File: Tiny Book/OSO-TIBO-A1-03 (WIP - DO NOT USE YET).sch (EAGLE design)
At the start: 103 parts, among them J2 10118193-0001LF, Q1 DMG341, Q2 IRLML0100, SW1 SPST_TACTILE_SWITCHRA-THRU, SW2 SPDT_SWITCH, U1 AP2112-3.3, U2 MCP73831T-2ACI/OT, U3 ATSAMD51G18A-MUT, U4 GD25Q16C (or GD25Q32C), U5 MAX4468EKAT, X1 JSTPH, X2 2x5 0.05" SWD

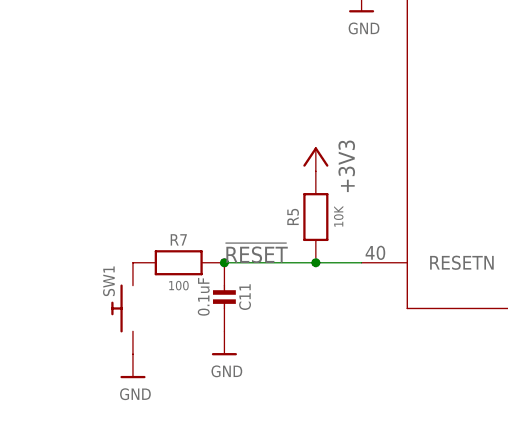
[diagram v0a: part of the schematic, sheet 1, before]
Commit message: surface mount reset button
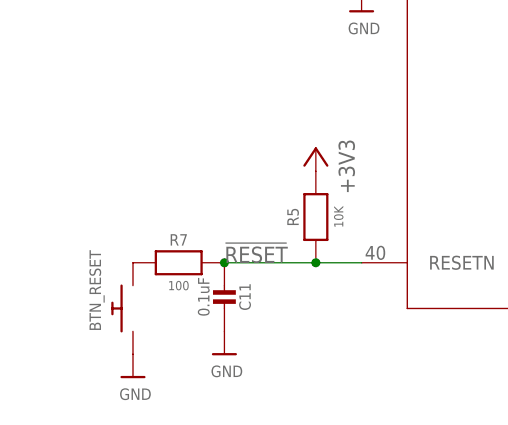
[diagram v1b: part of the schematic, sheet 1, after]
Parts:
- removed SW1: SPST_TACTILE_SWITCHRA-THRU, My Stuff:SPST_TACTILE_SWITCHRA-THRU
- added BTN_RESET: (no value), adafruit:SWITCH_PUSHBUTTONC&K_KSS
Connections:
- net GND: now also BTN_RESET.P$1; no longer SW1.P$1
- net N$1: now also BTN_RESET.P$2; no longer SW1.P$2
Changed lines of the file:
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@@
 <part name="SW2" library="My Stuff" deviceset="SPDT_SWITCH" device=""/>
 <part name="U$12" library="microbuilder" deviceset="GND" device=""/>
-<part name="SW1" library="My Stuff" deviceset="SPST_TACTILE_SWITCH" device="RA-THRU" value="SPST_TACTILE_SWITCHRA-THRU"/>
 <part name="+3V7" library="supply1" library_urn="urn:adsk.eagle:library:371" deviceset="+3V3" device=""/>
 <part name="+3V8" library="supply1" library_urn="urn:adsk.eagle:library:371" deviceset="+3V3" device=""/>
@@
 <part name="R5" library="microbuilder" deviceset="RESISTOR" device="0805_NOOUTLINE" value="10K"/>
 <part name="+3V6" library="supply1" library_urn="urn:adsk.eagle:library:371" deviceset="+3V3" device=""/>
+<part name="BTN_RESET" library="adafruit" deviceset="SWITCH_PUSHBUTTON" device="C&amp;K_KSS"/>
 </parts>
 <sheets>
@@
 <attribute name="VALUE" x="5.08" y="144.78" size="1.016" layer="96" font="vector" ratio="15" rot="R270" align="center"/>
 </instance>
-<instance part="SW1" gate="G$1" x="12.7" y="15.24" smashed="yes" rot="R90">
-<attribute name="NAME" x="10.668" y="16.51" size="1.27" layer="95" rot="R90"/>
-</instance>
 <instance part="U$24" gate="G$1" x="12.7" y="7.62" smashed="yes">
 <attribute name="VALUE" x="11.176" y="5.08" size="1.27" layer="96"/>
@@
 <instance part="+3V6" gate="G$1" x="33.02" y="33.02" smashed="yes" rot="MR0">
 <attribute name="VALUE" x="35.56" y="27.94" size="1.778" layer="96" rot="MR90"/>
+</instance>
+<instance part="BTN_RESET" gate="G$1" x="12.7" y="15.24" smashed="yes" rot="R90">
+<attribute name="NAME" x="9.144" y="12.7" size="1.27" layer="95" rot="R90"/>
+<attribute name="VALUE" x="14.986" y="12.7" size="1.27" layer="96" rot="R90"/>
 </instance>
 </instances>
@@
 <wire x1="238.76" y1="96.52" x2="243.84" y2="96.52" width="0.1524" layer="91"/>
 <junction x="243.84" y="96.52"/>
-</segment>
-<segment>
-<pinref part="U$24" gate="G$1" pin="GND"/>
-<pinref part="SW1" gate="G$1" pin="P$1"/>
 </segment>
 <segment>
@@
 <pinref part="U3" gate="A" pin="EPAD"/>
 <pinref part="U$3" gate="G$1" pin="GND"/>
+</segment>
+<segment>
+<pinref part="U$24" gate="G$1" pin="GND"/>
+<pinref part="BTN_RESET" gate="G$1" pin="P$1"/>
 </segment>
 </net>
@@
 </segment>
 </net>
-<net name="N$1" class="0">
-<segment>
-<pinref part="SW1" gate="G$1" pin="P$2"/>
-<pinref part="R7" gate="G$1" pin="1"/>
-</segment>
-</net>
 <net name="N$9" class="0">
 <segment>
@@
 </segment>
 </net>
+<net name="N$1" class="0">
+<segment>
+<pinref part="R7" gate="G$1" pin="1"/>
+<pinref part="BTN_RESET" gate="G$1" pin="P$2"/>
+</segment>
+</net>

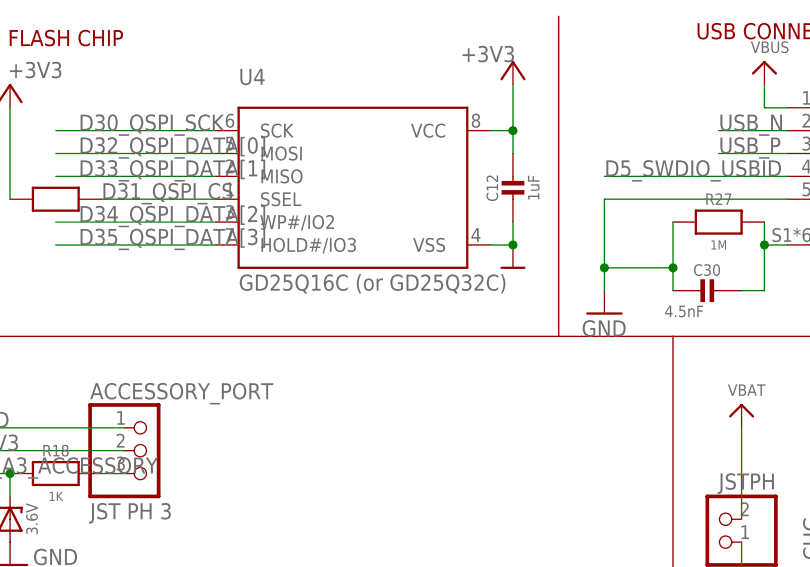
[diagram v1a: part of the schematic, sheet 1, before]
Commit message: use 4MB flash so babel can live there
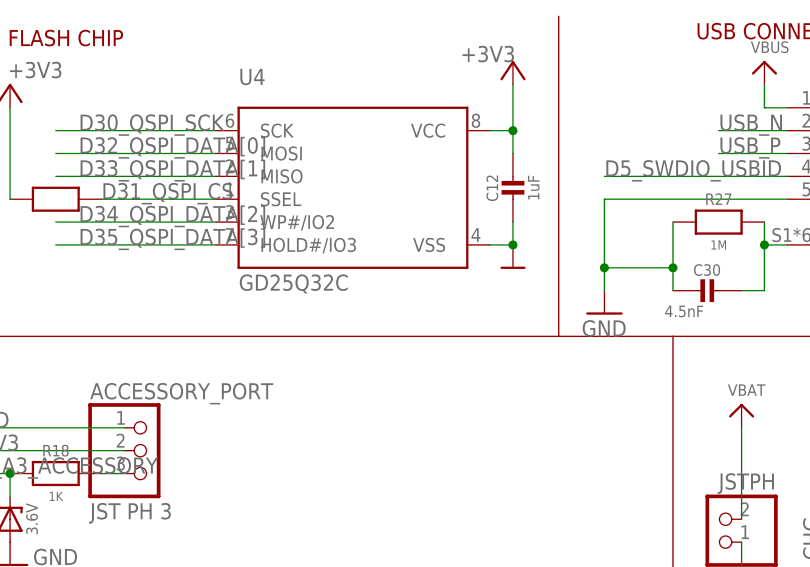
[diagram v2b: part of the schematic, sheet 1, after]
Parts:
- U4: value GD25Q16C (or GD25Q32C) -> GD25Q32C
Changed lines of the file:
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@@
 <part name="FID2" library="microbuilder" deviceset="FIDUCIAL" device="_1MM"/>
 <part name="U$24" library="microbuilder" deviceset="GND" device=""/>
-<part name="U4" library="Adafruit Feather M0 Express" deviceset="MICROBUILDER_SPIFLASH_SOIC8" device="" value="GD25Q16C (or GD25Q32C)"/>
+<part name="U4" library="Adafruit Feather M0 Express" deviceset="MICROBUILDER_SPIFLASH_SOIC8" device="" value="GD25Q32C"/>
 <part name="+3V15" library="supply1" library_urn="urn:adsk.eagle:library:371" deviceset="+3V3" device=""/>
 <part name="+3V16" library="supply1" library_urn="urn:adsk.eagle:library:371" deviceset="+3V3" device=""/>

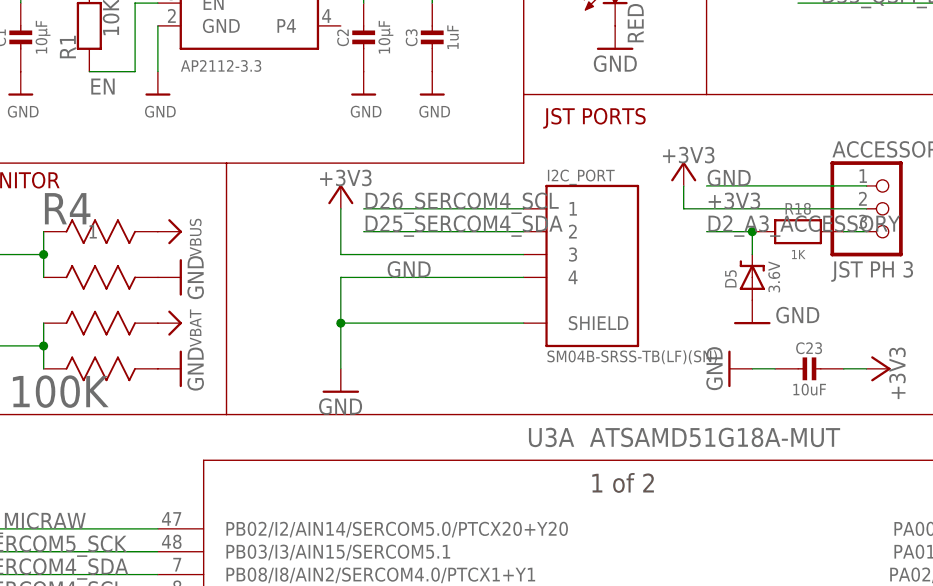
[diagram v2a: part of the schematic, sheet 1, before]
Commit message: fix I2C routing snafu
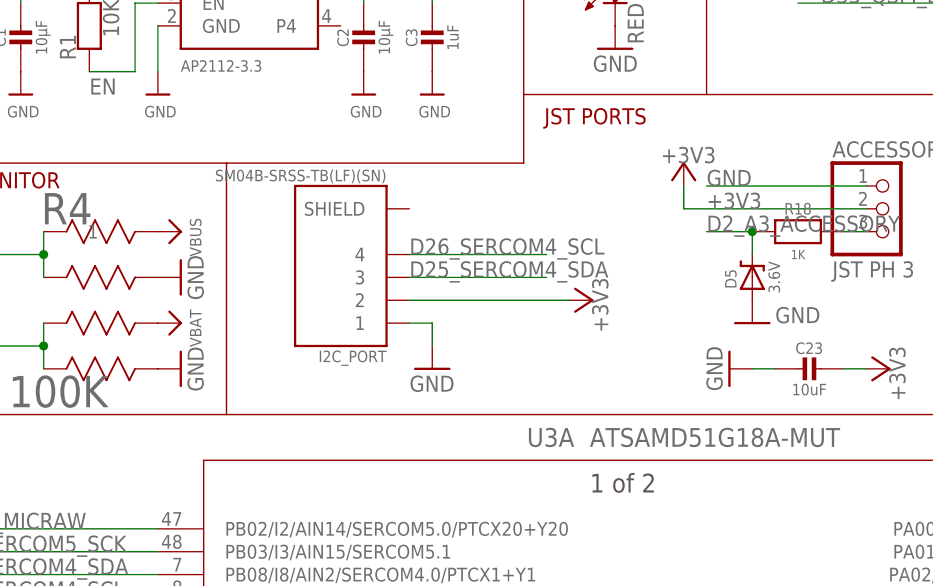
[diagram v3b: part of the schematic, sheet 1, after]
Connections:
- net +3V3: now also I2C_PORT.2; no longer I2C_PORT.3
- net D25_SERCOM4_SDA: now also I2C_PORT.3; no longer I2C_PORT.2
- net D26_SERCOM4_SCL: now also I2C_PORT.4; no longer I2C_PORT.1
- net GND: now also I2C_PORT.1; no longer I2C_PORT.4, I2C_PORT.SHIELD
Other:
- moved on the sheet: I2C_PORT
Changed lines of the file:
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@@
 <part name="+3V8" library="supply1" library_urn="urn:adsk.eagle:library:371" deviceset="+3V3" device=""/>
 <part name="GND1" library="supply1" deviceset="GND" device=""/>
-<part name="GND5" library="supply1" deviceset="GND" device=""/>
 <part name="FRAME2" library="My Stuff" deviceset="A4L-LOC" device=""/>
 <part name="JP1" library="adafruit" deviceset="PINHD-1X3" device=""/>
@@
 <part name="+3V3" library="supply1" library_urn="urn:adsk.eagle:library:371" deviceset="+3V3" device=""/>
 <part name="GOLD_ORB_SM1" library="oshw" deviceset="OSHWLOGO" device="LOGO5MM"/>
-<part name="+3V4" library="supply1" library_urn="urn:adsk.eagle:library:371" deviceset="+3V3" device=""/>
 <part name="+3V13" library="supply1" library_urn="urn:adsk.eagle:library:371" deviceset="+3V3" device=""/>
 <part name="U$1" library="microbuilder" deviceset="MOUNTINGHOLE" device="2.5" value="MOUNTINGHOLE2.5"/>
@@
 <part name="+3V6" library="supply1" library_urn="urn:adsk.eagle:library:371" deviceset="+3V3" device=""/>
 <part name="BTN_RESET" library="adafruit" deviceset="SWITCH_PUSHBUTTON" device="C&amp;K_KSS"/>
+<part name="+3V9" library="supply1" library_urn="urn:adsk.eagle:library:371" deviceset="+3V3" device=""/>
+<part name="GND9" library="supply1" deviceset="GND" device=""/>
 </parts>
 <sheets>
@@
 <attribute name="VALUE" x="99.06" y="111.76" size="1.778" layer="96" rot="R270"/>
 </instance>
-<instance part="GND5" gate="1" x="58.42" y="106.68" smashed="yes">
-<attribute name="VALUE" x="55.88" y="104.14" size="1.778" layer="96"/>
-</instance>
 <instance part="+3V3" gate="G$1" x="119.38" y="109.22" smashed="yes" rot="R270">
 <attribute name="VALUE" x="119.38" y="111.76" size="1.778" layer="96" rot="R270"/>
 </instance>
-<instance part="+3V4" gate="G$1" x="58.42" y="129.54" smashed="yes">
-<attribute name="VALUE" x="55.88" y="129.54" size="1.778" layer="96"/>
-</instance>
 <instance part="+3V13" gate="G$1" x="96.52" y="132.08" smashed="yes">
 <attribute name="VALUE" x="93.98" y="132.08" size="1.778" layer="96"/>
 </instance>
-<instance part="I2C_PORT" gate="G$2" x="86.36" y="121.92" smashed="yes">
-<attribute name="NAME" x="81.276940625" y="130.0633" size="1.27153125" layer="95"/>
-<attribute name="VALUE" x="81.276459375" y="109.9643" size="1.27176875" layer="96"/>
+<instance part="I2C_PORT" gate="G$2" x="58.42" y="119.38" smashed="yes" rot="R180">
+<attribute name="NAME" x="63.503059375" y="111.2367" size="1.27153125" layer="95" rot="R180"/>
+<attribute name="VALUE" x="63.503540625" y="131.3357" size="1.27176875" layer="96" rot="R180"/>
 </instance>
 <instance part="U4" gate="G$1" x="142.24" y="154.94" smashed="yes">
@@
 <attribute name="NAME" x="9.144" y="12.7" size="1.27" layer="95" rot="R90"/>
 <attribute name="VALUE" x="14.986" y="12.7" size="1.27" layer="96" rot="R90"/>
+</instance>
+<instance part="+3V9" gate="G$1" x="86.36" y="116.84" smashed="yes" rot="R270">
+<attribute name="VALUE" x="86.36" y="119.38" size="1.778" layer="96" rot="R270"/>
+</instance>
+<instance part="GND9" gate="1" x="68.58" y="109.22" smashed="yes">
+<attribute name="VALUE" x="66.04" y="106.68" size="1.778" layer="96"/>
 </instance>
 </instances>
@@
 <wire x1="182.88" y1="99.06" x2="182.88" y2="96.52" width="0.1524" layer="91"/>
 <pinref part="U$57" gate="G$1" pin="GND"/>
-</segment>
-<segment>
-<label x="63.5" y="119.38" size="1.778" layer="95"/>
-<wire x1="78.74" y1="119.38" x2="58.42" y2="119.38" width="0.1524" layer="91"/>
-<wire x1="58.42" y1="119.38" x2="58.42" y2="114.3" width="0.1524" layer="91"/>
-<pinref part="GND5" gate="1" pin="GND"/>
-<pinref part="I2C_PORT" gate="G$2" pin="4"/>
-<pinref part="I2C_PORT" gate="G$2" pin="SHIELD"/>
-<wire x1="58.42" y1="114.3" x2="58.42" y2="109.22" width="0.1524" layer="91"/>
-<wire x1="78.74" y1="114.3" x2="58.42" y2="114.3" width="0.1524" layer="91"/>
-<junction x="58.42" y="114.3"/>
 </segment>
 <segment>
@@
 <pinref part="BTN_RESET" gate="G$1" pin="P$1"/>
 </segment>
+<segment>
+<pinref part="I2C_PORT" gate="G$2" pin="1"/>
+<pinref part="GND9" gate="1" pin="GND"/>
+<wire x1="66.04" y1="114.3" x2="68.58" y2="114.3" width="0.1524" layer="91"/>
+<wire x1="68.58" y1="114.3" x2="68.58" y2="111.76" width="0.1524" layer="91"/>
+</segment>
 </net>
 <net name="EN" class="0">
@@
 <pinref part="+3V3" gate="G$1" pin="+3V3"/>
 <wire x1="116.84" y1="109.22" x2="114.3" y2="109.22" width="0.1524" layer="91"/>
-</segment>
-<segment>
-<wire x1="78.74" y1="121.92" x2="58.42" y2="121.92" width="0.1524" layer="91"/>
-<wire x1="58.42" y1="121.92" x2="58.42" y2="127" width="0.1524" layer="91"/>
-<pinref part="+3V4" gate="G$1" pin="+3V3"/>
-<pinref part="I2C_PORT" gate="G$2" pin="3"/>
 </segment>
 <segment>
@@
 <pinref part="+3V6" gate="G$1" pin="+3V3"/>
 </segment>
+<segment>
+<pinref part="I2C_PORT" gate="G$2" pin="2"/>
+<pinref part="+3V9" gate="G$1" pin="+3V3"/>
+<wire x1="83.82" y1="116.84" x2="66.04" y2="116.84" width="0.1524" layer="91"/>
+</segment>
 </net>
 <net name="D10_EINK_DC" class="0">
@@
 </segment>
 <segment>
-<wire x1="78.74" y1="124.46" x2="60.96" y2="124.46" width="0.1524" layer="91"/>
-<label x="60.96" y="124.46" size="1.778" layer="95"/>
-<pinref part="I2C_PORT" gate="G$2" pin="2"/>
+<label x="66.04" y="119.38" size="1.778" layer="95"/>
+<wire x1="81.28" y1="119.38" x2="66.04" y2="119.38" width="0.1524" layer="91"/>
+<pinref part="I2C_PORT" gate="G$2" pin="3"/>
 </segment>
 </net>
@@
 </segment>
 <segment>
-<wire x1="78.74" y1="127" x2="60.96" y2="127" width="0.1524" layer="91"/>
-<label x="60.96" y="127" size="1.778" layer="95"/>
-<pinref part="I2C_PORT" gate="G$2" pin="1"/>
-</segment>
-</net>
+<label x="66.04" y="121.92" size="1.778" layer="95"/>
+<wire x1="81.28" y1="121.92" x2="66.04" y2="121.92" width="0.1524" layer="91"/>
+<pinref part="I2C_PORT" gate="G$2" pin="4"/>
+</segment>
+</net>
